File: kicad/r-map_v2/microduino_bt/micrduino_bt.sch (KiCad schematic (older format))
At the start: 13 parts, among them P1 CONN_01X01, P2 CONN_01X01, P3 CONN_01X01, P4 CONN_01X01, P5 CONN_01X01, P6 CONN_01X01, U1 Microduino, U2 ITEAD_HC-05

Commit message: Add files from last commit on sourceforge
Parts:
- removed P1, P2, P4, P5, P6: CONN_01X01, Measurement_Points:Measurement_Point_Square-SMD-Pad_Small, symbol CONN_01X01
- removed R4: 10K, w_smd_resistors:r_0805, symbol R
- added P?: CONN_01X01, Measurement_Points:Measurement_Point_Square-SMD-Pad_Small, symbol CONN_01X01
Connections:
- net RX1: now reaches U1.7 (D2), U2.1 (UART_TX)
- net LED: now reaches U2.24 (PIO1)
- net LED: now also D1.2 (A), U2.31 (PIO8)
- net SET: now reaches P3.1 (P1), U2.34 (PIO11)
- net SCL: now reaches U1.12 (A5)
- net SDA: now reaches U1.13 (A4)
- net SCK: now reaches U1.19 (D13)
- net MISO: now reaches U1.20 (D12)
- net MOSI: now reaches U1.21 (D11)
- net CS_NRF24: now reaches U1.22 (D10)
- net CE_NRF24: now reaches U1.23 (D9)
- net CONFIG: now reaches U1.24 (D8)
- net INT_28J60: now reaches R1.1, U1.6 (D3)
- no-connect marks 46 -> 47
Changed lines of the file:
@@
-	1    0    0    -1
-$EndComp
-$Comp
-L R R4
-U 1 1 55008D30
-P 5000 2900
-F 0 "R4" V 5080 2900 40  0000 C CNN
-F 1 "10K" V 5007 2901 40  0000 C CNN
-F 2 "w_smd_resistors:r_0805" V 4930 2900 30  0001 C CNN
-F 3 "" H 5000 2900 30  0000 C CNN
-	1    5000 2900
 	1    0    0    -1
 $EndComp
@@
 $EndComp
 $Comp
-L CONN_01X01 P1
-U 1 1 5502DA26
-P 4900 2050
-F 0 "P1" H 4950 2100 60  0001 C CNN
-F 1 "CONN_01X01" H 4900 2050 60  0001 C CNN
-F 2 "Measurement_Points:Measurement_Point_Square-SMD-Pad_Small" H 4900 2050 60  0001 C CNN
-F 3 "" H 4900 2050 60  0001 C CNN
-F 4 "P" H 4900 2150 50  0000 C CNN "Riferimento"
-F 5 "CONN_01X01" V 5000 2050 50  0000 C CNN "Valore "
-F 6 "" H 4900 2050 60  0000 C CNN "Impronta"
-F 7 "" H 4900 2050 60  0000 C CNN "Specifiche"
-	1    4900 2050
-	0    -1   -1   0
-$EndComp
-$Comp
-L CONN_01X01 P2
-U 1 1 5502DA52
-P 5000 2050
-F 0 "P2" H 5050 2100 60  0001 C CNN
-F 1 "CONN_01X01" H 5000 2050 60  0001 C CNN
-F 2 "Measurement_Points:Measurement_Point_Square-SMD-Pad_Small" H 5000 2050 60  0001 C CNN
-F 3 "" H 5000 2050 60  0001 C CNN
-F 4 "P" H 5000 2150 50  0000 C CNN "Riferimento"
-F 5 "CONN_01X01" V 5100 2050 50  0000 C CNN "Valore "
-F 6 "" H 5000 2050 60  0000 C CNN "Impronta"
-F 7 "" H 5000 2050 60  0000 C CNN "Specifiche"
-	1    5000 2050
-	0    -1   -1   0
-$EndComp
-$Comp
 L CONN_01X01 P3
 U 1 1 5502DA6A
-P 5100 2050
-F 0 "P3" H 5150 2100 60  0001 C CNN
-F 1 "CONN_01X01" H 5100 2050 60  0001 C CNN
-F 2 "Measurement_Points:Measurement_Point_Square-SMD-Pad_Small" H 5100 2050 60  0001 C CNN
-F 3 "" H 5100 2050 60  0001 C CNN
-F 4 "P" H 5100 2150 50  0000 C CNN "Riferimento"
-F 5 "CONN_01X01" V 5200 2050 50  0000 C CNN "Valore "
-F 6 "" H 5100 2050 60  0000 C CNN "Impronta"
-F 7 "" H 5100 2050 60  0000 C CNN "Specifiche"
-	1    5100 2050
-	0    -1   -1   0
-$EndComp
-$Comp
-L CONN_01X01 P4
-U 1 1 5502DA85
-P 5500 2050
-F 0 "P4" H 5550 2100 60  0001 C CNN
-F 1 "CONN_01X01" H 5500 2050 60  0001 C CNN
-F 2 "Measurement_Points:Measurement_Point_Square-SMD-Pad_Small" H 5500 2050 60  0001 C CNN
-F 3 "" H 5500 2050 60  0001 C CNN
-F 4 "P" H 5500 2150 50  0000 C CNN "Riferimento"
-F 5 "CONN_01X01" V 5600 2050 50  0000 C CNN "Valore "
-F 6 "" H 5500 2050 60  0000 C CNN "Impronta"
-F 7 "" H 5500 2050 60  0000 C CNN "Specifiche"
-	1    5500 2050
-	0    -1   -1   0
-$EndComp
-$Comp
-L CONN_01X01 P5
-U 1 1 5502DAB1
-P 5600 2050
-F 0 "P5" H 5650 2100 60  0001 C CNN
-F 1 "CONN_01X01" H 5600 2050 60  0001 C CNN
-F 2 "Measurement_Points:Measurement_Point_Square-SMD-Pad_Small" H 5600 2050 60  0001 C CNN
-F 3 "" H 5600 2050 60  0001 C CNN
-F 4 "P" H 5600 2150 50  0000 C CNN "Riferimento"
-F 5 "CONN_01X01" V 5700 2050 50  0000 C CNN "Valore "
-F 6 "" H 5600 2050 60  0000 C CNN "Impronta"
-F 7 "" H 5600 2050 60  0000 C CNN "Specifiche"
-	1    5600 2050
-	0    -1   -1   0
-$EndComp
-$Comp
-L CONN_01X01 P6
-U 1 1 5502DAC9
-P 5700 2050
-F 0 "P6" H 5750 2100 60  0001 C CNN
-F 1 "CONN_01X01" H 5700 2050 60  0001 C CNN
-F 2 "Measurement_Points:Measurement_Point_Square-SMD-Pad_Small" H 5700 2050 60  0001 C CNN
-F 3 "" H 5700 2050 60  0001 C CNN
-F 4 "P" H 5700 2150 50  0000 C CNN "Riferimento"
-F 5 "CONN_01X01" V 5800 2050 50  0000 C CNN "Valore "
-F 6 "" H 5700 2050 60  0000 C CNN "Impronta"
-F 7 "" H 5700 2050 60  0000 C CNN "Specifiche"
-	1    5700 2050
-	0    -1   -1   0
+P 5050 3500
+F 0 "P3" H 5100 3550 60  0001 C CNN
+F 1 "CONN_01X01" H 5050 3500 60  0001 C CNN
+F 2 "Measurement_Points:Measurement_Point_Square-SMD-Pad_Small" H 5050 3500 60  0001 C CNN
+F 3 "" H 5050 3500 60  0001 C CNN
+F 4 "P" H 5050 3600 50  0000 C CNN "Riferimento"
+F 5 "CONN_01X01" V 5150 3500 50  0000 C CNN "Valore "
+F 6 "" H 5050 3500 60  0000 C CNN "Impronta"
+F 7 "" H 5050 3500 60  0000 C CNN "Specifiche"
+	1    5050 3500
+	1    0    0    -1
 $EndComp
 Wire Wire Line
 	4000 3900 4000 3750
 Wire Wire Line
-	4100 3750 4100 3900
-Wire Wire Line
-	4100 3900 4100 4000
+	4100 3750 4100 4000
 Wire Wire Line
 	4200 3900 4200 3750
@@
 Connection ~ 4200 3900
 Wire Wire Line
-	5100 3500 4700 3500
-Wire Wire Line
 	3250 3750 3250 3900
 Connection ~ 3250 3900
@@
 	1250 3300 3250 3300
 Wire Wire Line
-	3250 2350 3250 3300
-Wire Wire Line
-	3250 3300 3250 3450
+	3250 2350 3250 3450
 Connection ~ 3250 3300
 Wire Wire Line
-	5000 2250 5000 2750
-Wire Wire Line
-	1150 3900 3250 3900
-Wire Wire Line
-	3250 3900 4000 3900
-Wire Wire Line
-	4000 3900 4100 3900
-Wire Wire Line
-	4100 3900 4200 3900
-Wire Wire Line
-	4200 3900 5000 3900
-Wire Wire Line
-	5000 3900 5600 3900
-Wire Wire Line
-	5700 3200 4700 3200
-Wire Wire Line
-	5600 2250 5600 2700
+	1150 3900 5600 3900
 Wire Wire Line
 	5600 3100 5600 3450
 Wire Wire Line
 	5600 3900 5600 3750
-Connection ~ 5000 3900
 Wire Wire Line
-	4700 2700 4900 2700
-Wire Wire Line
-	4900 2700 4900 2250
-Wire Wire Line
-	5100 2250 5100 3500
-Wire Wire Line
-	5500 2250 5500 2500
-Wire Wire Line
-	5500 2500 4700 2500
-Wire Wire Line
-	5000 3050 5000 3900
-Wire Wire Line
-	5700 2250 5700 3200
+	4700 2500 5600 2500
 Wire Wire Line
 	2850 1750 4100 1750
@@
 NoConn ~ 1450 2350
 NoConn ~ 1450 2450
+Wire Wire Line
+	5600 2500 5600 2700
+Wire Wire Line
+	4700 3200 5300 3200
+Wire Wire Line
+	5300 3200 5300 2500
+Connection ~ 5300 2500
+NoConn ~ 4700 2700
+Wire Wire Line
+	4850 3500 4700 3500
+Text Label 4750 3500 0    60   ~ 0
+SET
+Text Label 4900 3200 0    60   ~ 0
+LED
+Text Label 1950 2850 3    60   ~ 0
+SCL
+Text Label 2050 2850 3    60   ~ 0
+SDA
+Text Label 2850 2450 0    60   ~ 0
+SCK
+Text Label 2850 2350 0    60   ~ 0
+MISO
+Text Label 2850 2250 0    60   ~ 0
+MOSI
+Text Label 2850 2150 0    60   ~ 0
+CS_NRF24
+Text Label 2850 2050 0    60   ~ 0
+CE_NRF24
+Text Label 2850 1950 0    60   ~ 0
+CS_ENC28J60
+Text Label 1450 2250 2    60   ~ 0
+RX1
+Text Label 1400 2150 2    60   ~ 0
+TX1
+Text Label 1250 2150 2    60   ~ 0
+INT_28J60
+Text Label 2850 1950 2    60   ~ 0
+CONFIG
+$Comp
+L CONN_01X01 P?
+U 1 1 55A299C8
+P 5050 3700
+F 0 "P?" H 5100 3750 60  0001 C CNN
+F 1 "CONN_01X01" H 5050 3700 60  0001 C CNN
+F 2 "Measurement_Points:Measurement_Point_Square-SMD-Pad_Small" H 5050 3700 60  0001 C CNN
+F 3 "" H 5050 3700 60  0001 C CNN
+F 4 "P" H 5050 3800 50  0000 C CNN "Riferimento"
+F 5 "CONN_01X01" V 5150 3700 50  0000 C CNN "Valore "
+F 6 "" H 5050 3700 60  0000 C CNN "Impronta"
+F 7 "" H 5050 3700 60  0000 C CNN "Specifiche"
+	1    5050 3700
+	1    0    0    -1
+$EndComp
 $EndSCHEMATC

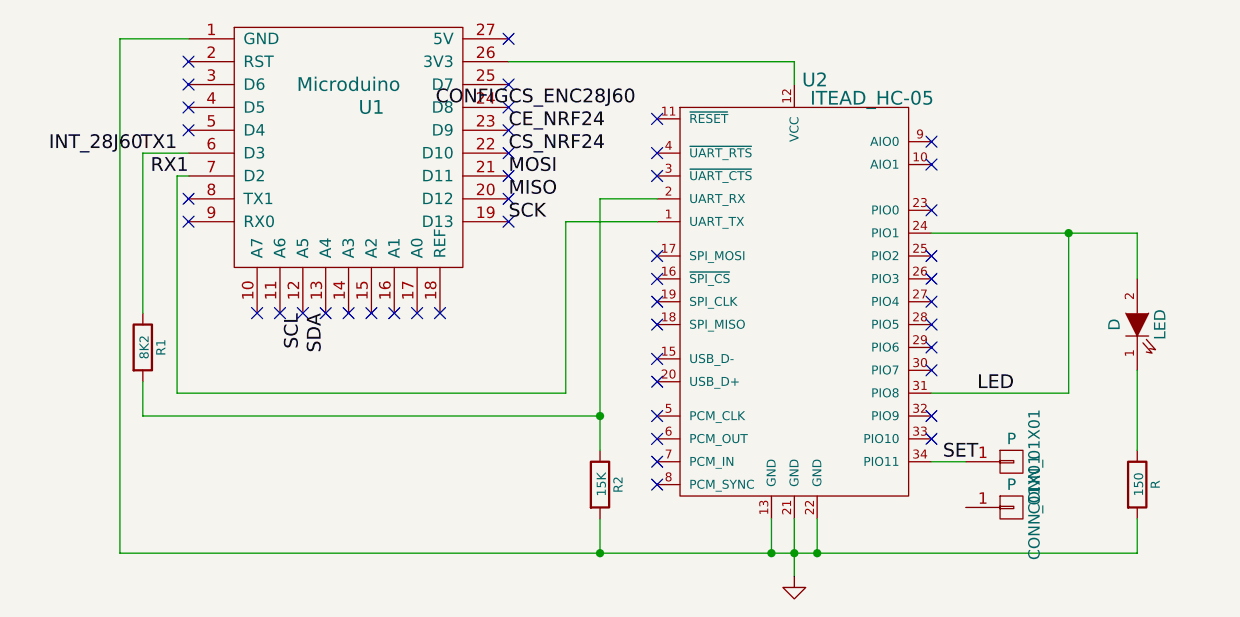
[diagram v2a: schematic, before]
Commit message: Modifiche a schema elettrico su modulo bluethoot, modificate connessioni per seriale 1. Modulo stima-i2c modificati pin per rele' e aggiunte connessioni esd su alimentazione. Rigenerati pcb.
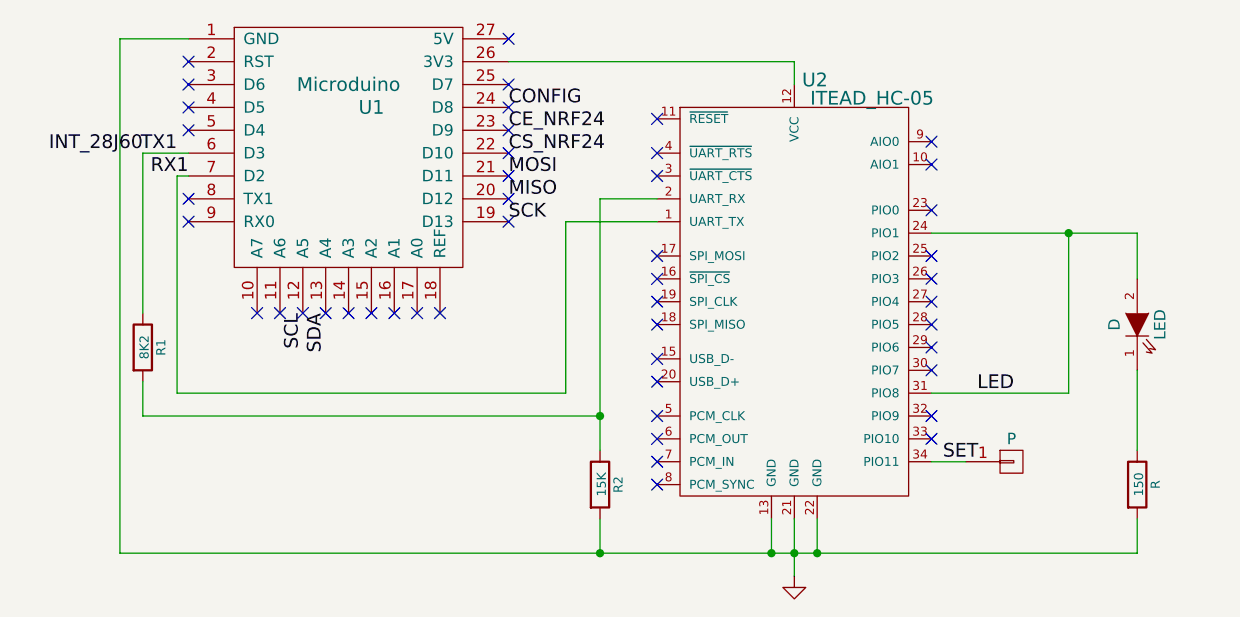
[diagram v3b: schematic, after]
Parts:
- removed P?: CONN_01X01, Measurement_Points:Measurement_Point_Square-SMD-Pad_Small, symbol CONN_01X01
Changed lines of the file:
@@
 F 3 "" H 5050 3500 60  0001 C CNN
 F 4 "P" H 5050 3600 50  0000 C CNN "Riferimento"
-F 5 "CONN_01X01" V 5150 3500 50  0000 C CNN "Valore "
+F 5 "CONN_01X01" V 5150 3500 50  0001 C CNN "Valore "
 F 6 "" H 5050 3500 60  0000 C CNN "Impronta"
 F 7 "" H 5050 3500 60  0000 C CNN "Specifiche"
@@
 Text Label 2050 2850 3    60   ~ 0
 SDA
+Text Label 1450 2250 2    60   ~ 0
+RX1
+Text Label 1400 2150 2    60   ~ 0
+TX1
+Text Label 2850 1950 0    60   ~ 0
+CONFIG
 Text Label 2850 2450 0    60   ~ 0
 SCK
@@
 Text Label 2850 2050 0    60   ~ 0
 CE_NRF24
-Text Label 2850 1950 0    60   ~ 0
-CS_ENC28J60
-Text Label 1450 2250 2    60   ~ 0
-RX1
-Text Label 1400 2150 2    60   ~ 0
-TX1
 Text Label 1250 2150 2    60   ~ 0
 INT_28J60
-Text Label 2850 1950 2    60   ~ 0
-CONFIG
-$Comp
-L CONN_01X01 P?
-U 1 1 55A299C8
-P 5050 3700
-F 0 "P?" H 5100 3750 60  0001 C CNN
-F 1 "CONN_01X01" H 5050 3700 60  0001 C CNN
-F 2 "Measurement_Points:Measurement_Point_Square-SMD-Pad_Small" H 5050 3700 60  0001 C CNN
-F 3 "" H 5050 3700 60  0001 C CNN
-F 4 "P" H 5050 3800 50  0000 C CNN "Riferimento"
-F 5 "CONN_01X01" V 5150 3700 50  0000 C CNN "Valore "
-F 6 "" H 5050 3700 60  0000 C CNN "Impronta"
-F 7 "" H 5050 3700 60  0000 C CNN "Specifiche"
-	1    5050 3700
-	1    0    0    -1
-$EndComp
 $EndSCHEMATC

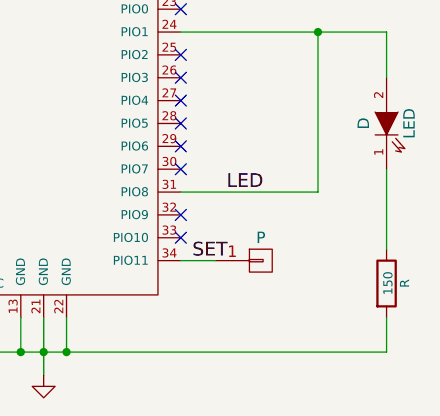
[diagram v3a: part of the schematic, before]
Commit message: Sistemato orientamento case led smd, generati files gbr per i2c hub e breakout board
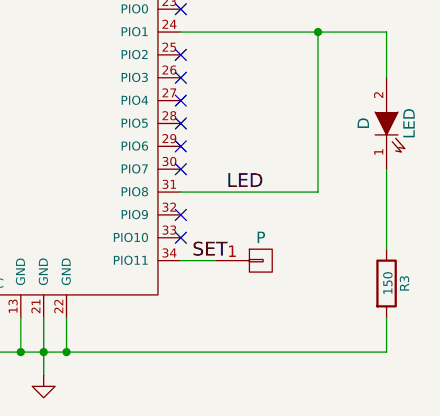
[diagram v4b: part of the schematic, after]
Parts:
- R3: Riferimento R -> R3
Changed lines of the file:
@@
 F 2 "w_smd_resistors:r_0805" H 5600 3600 60  0001 C CNN
 F 3 "" H 5600 3600 60  0001 C CNN
-F 4 "R" V 5680 3600 40  0000 C CNN "Riferimento"
+F 4 "R3" V 5680 3600 40  0000 C CNN "Riferimento"
 F 5 "150" V 5607 3601 40  0000 C CNN "Valore "
 	1    5600 3600

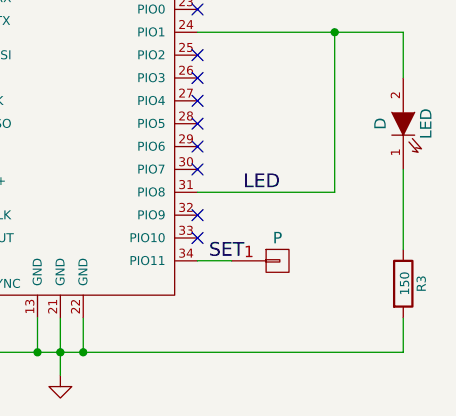
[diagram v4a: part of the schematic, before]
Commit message: Aggiornamento files gerber e verifica per nuova stampa pcb, revisionate tutte e 4 le board. Il file kicad/r-map_v2/futura_10-2015.zip contiene i files divisi per cartelle di tutte le board
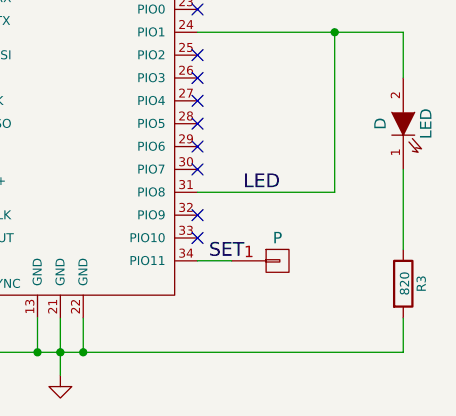
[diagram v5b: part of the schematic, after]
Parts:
- R3: Valore  150 -> 820
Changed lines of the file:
@@
 F 3 "" H 5600 3600 60  0001 C CNN
 F 4 "R3" V 5680 3600 40  0000 C CNN "Riferimento"
-F 5 "150" V 5607 3601 40  0000 C CNN "Valore "
+F 5 "820" V 5607 3601 40  0000 C CNN "Valore "
 	1    5600 3600
 	1    0    0    -1
